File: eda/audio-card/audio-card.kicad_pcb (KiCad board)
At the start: 2 copper layers, 182.4 x 99.1 mm, 13 parts, among them J1 AudioJack2_SwitchT, J2 Bus expansion

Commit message: Interim commit
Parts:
- added U2: 74LS593, Package_DIP:DIP-20_W7.62mm, F.Cu at (100.6, 59.6)
- added U3: 74HCT138, Package_DIP:DIP-16_W10.16mm, F.Cu at (139.7, 125.2)
- added U4: 74HCT574, Package_DIP:DIP-20_W7.62mm, F.Cu at (111.5, 59.6)
- added U5: 74LS593, Package_DIP:DIP-20_W7.62mm, F.Cu at (122.3, 59.6)
- added U6: 74HCT574, Package_DIP:DIP-20_W7.62mm, F.Cu at (133.2, 59.6)
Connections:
- J2 pad 10: /Expansion/D3 -> /Channel/D3
- J2 pad 12: /Expansion/D4 -> /Channel/D4
- J2 pad 14: /Expansion/D5 -> /Channel/D5
- J2 pad 16: /Expansion/D6 -> /Channel/D6
- J2 pad 18: /Expansion/D7 -> /Channel/D7
- J2 pad 36: /Expansion/~{RST} -> /Channel/~{Reset}
- J2 pad 4: /Expansion/D0 -> /Channel/D0
- J2 pad 6: /Expansion/D1 -> /Channel/D1
- J2 pad 8: /Expansion/D2 -> /Channel/D2
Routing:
- net /Expansion/Clock: track 2.79 -> 68.6 mm
- net /Expansion/R~{W}: track 2.79 -> 64.8 mm
- net /Expansion/~{CS}: track 26.7 -> 58.2 mm
- net /Channel/D0: track 0.00 -> 10.7 mm
- net /Channel/D1: track 0.00 -> 10.4 mm
- net /Channel/D3: track 0.00 -> 10.1 mm
- net /Channel/D2: track 0.00 -> 10.1 mm
- net /Channel/D4: track 0.00 -> 9.88 mm
- net /Channel/D5: track 0.00 -> 9.73 mm
- net /Channel/D6: track 0.00 -> 9.48 mm
- net /Channel/D7: track 0.00 -> 9.12 mm
- net /Expansion/A2: track 2.79 -> 11.4 mm
- net /Expansion/A1: track 2.79 -> 11.4 mm
- net /Expansion/A0: track 2.79 -> 11.4 mm
- net /Expansion/D0: track 6.37 -> 0.00 mm
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
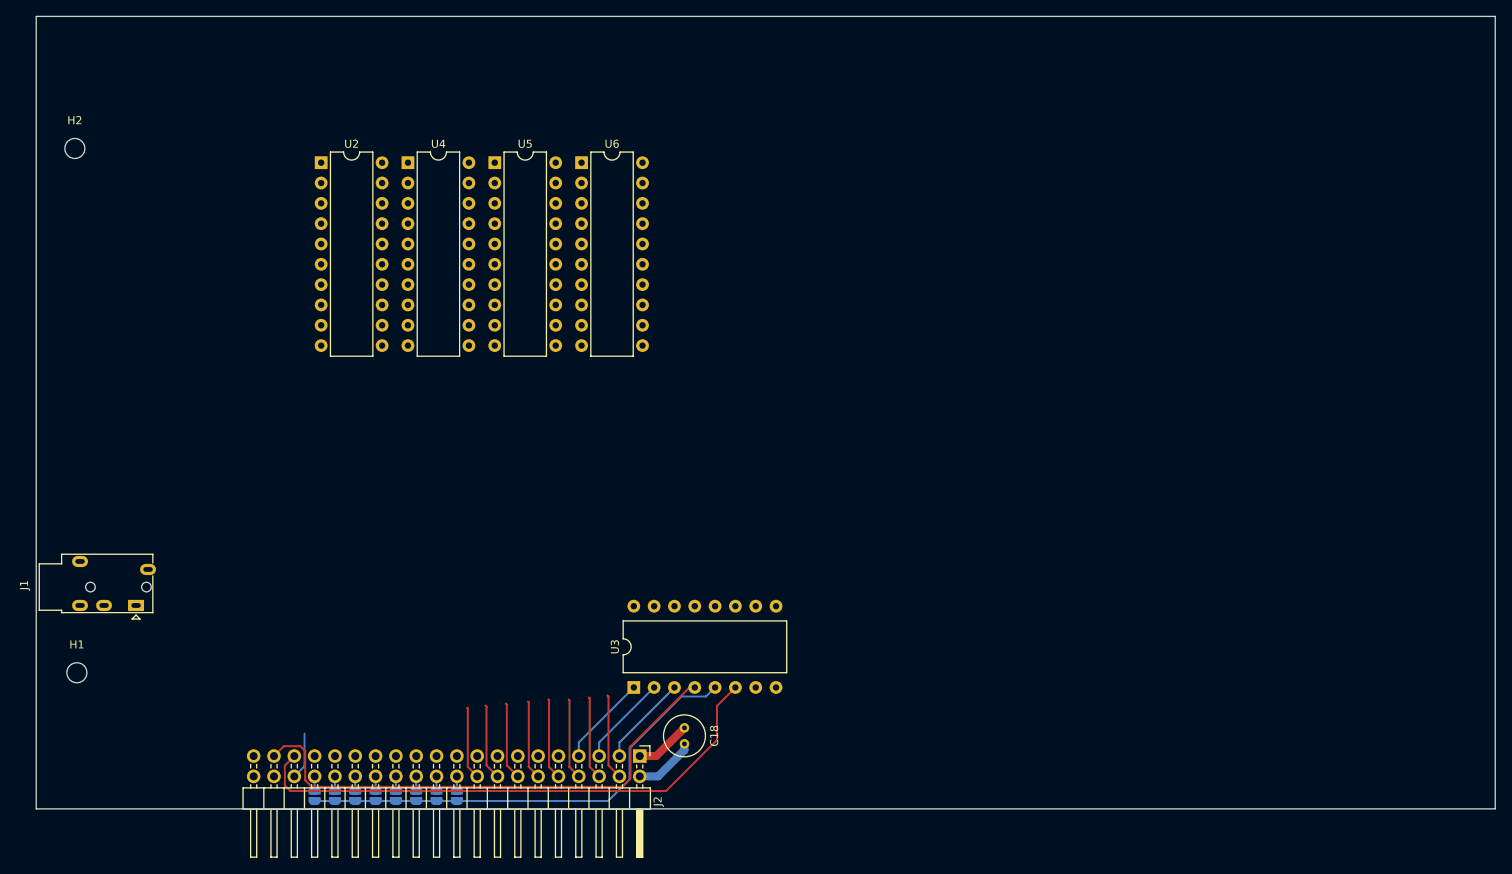
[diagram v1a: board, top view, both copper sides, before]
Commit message: Start converting audio card to analog synth base
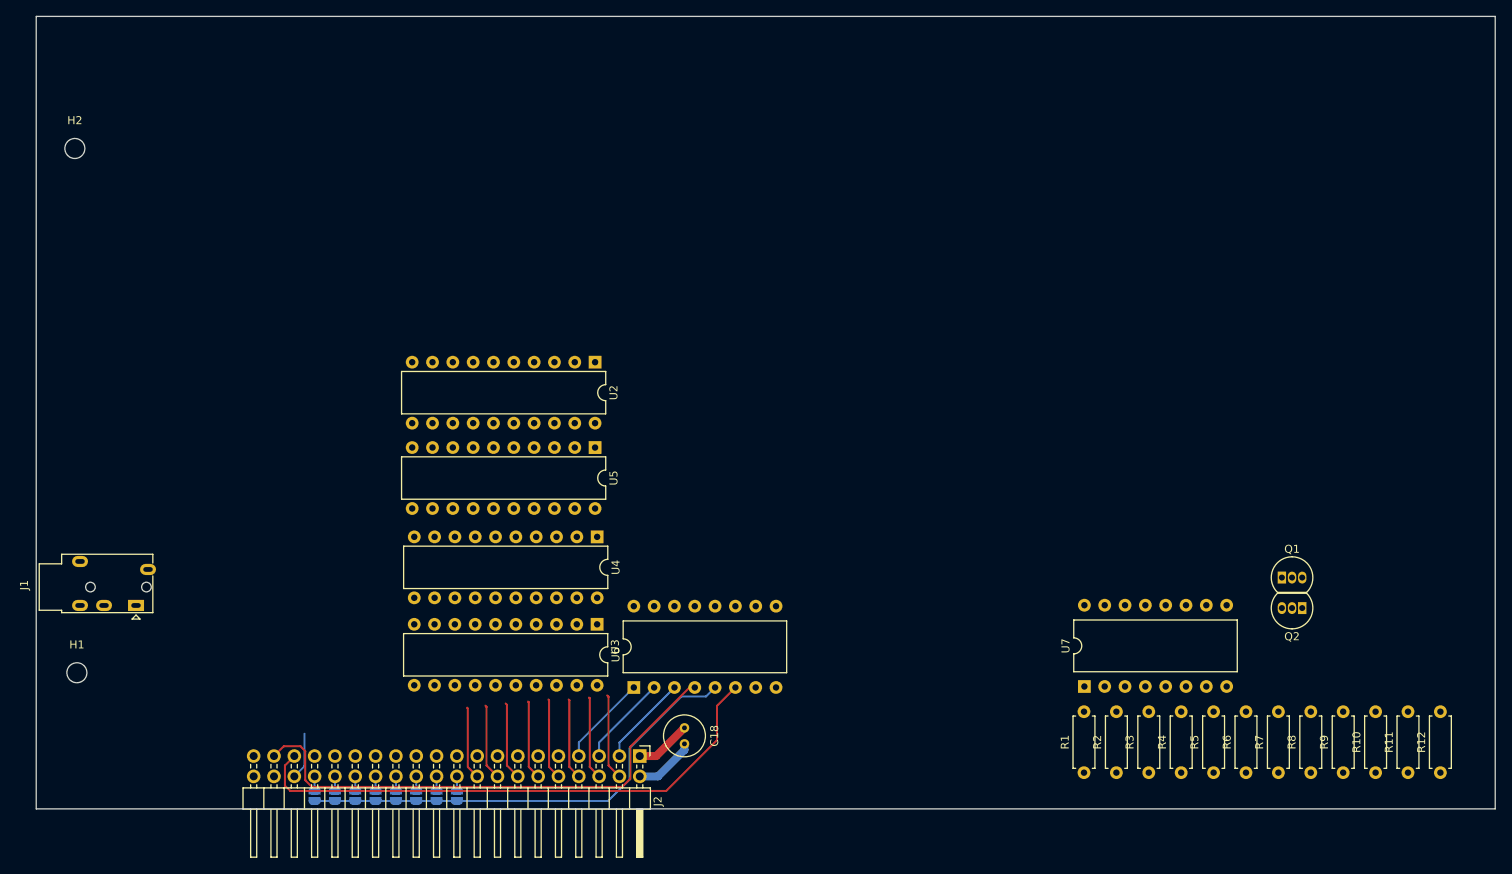
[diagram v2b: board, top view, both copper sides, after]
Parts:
- added Q1: BC558, Package_TO_SOT_THT:TO-92_Inline, F.Cu at (220.7, 111.5)
- added Q2: BC558, Package_TO_SOT_THT:TO-92_Inline, F.Cu at (223.3, 115.3)
- added R1: 100k, Resistor_THT:R_Axial_DIN0207_L6.3mm_D2.5mm_P7.62mm_Horizontal, F.Cu at (196.0, 135.9)
- added R10: 470k, Resistor_THT:R_Axial_DIN0207_L6.3mm_D2.5mm_P7.62mm_Horizontal, F.Cu at (232.4, 135.9)
- added R11: 470k, Resistor_THT:R_Axial_DIN0207_L6.3mm_D2.5mm_P7.62mm_Horizontal, F.Cu at (236.5, 135.9)
- added R12: 1k, Resistor_THT:R_Axial_DIN0207_L6.3mm_D2.5mm_P7.62mm_Horizontal, F.Cu at (240.5, 135.9)
- added R2: 100k, Resistor_THT:R_Axial_DIN0207_L6.3mm_D2.5mm_P7.62mm_Horizontal, F.Cu at (200.0, 135.9)
- added R3: 100k, Resistor_THT:R_Axial_DIN0207_L6.3mm_D2.5mm_P7.62mm_Horizontal, F.Cu at (204.1, 135.9)
- added R4: 100R, Resistor_THT:R_Axial_DIN0207_L6.3mm_D2.5mm_P7.62mm_Horizontal, F.Cu at (208.1, 135.9)
- added R5: 200k, Resistor_THT:R_Axial_DIN0207_L6.3mm_D2.5mm_P7.62mm_Horizontal, F.Cu at (212.2, 135.9)
- added R6: 33k, Resistor_THT:R_Axial_DIN0207_L6.3mm_D2.5mm_P7.62mm_Horizontal, F.Cu at (216.2, 135.9)
- added R7: 10k, Resistor_THT:R_Axial_DIN0207_L6.3mm_D2.5mm_P7.62mm_Horizontal, F.Cu at (220.3, 135.9)
- added R8: 10k, Resistor_THT:R_Axial_DIN0207_L6.3mm_D2.5mm_P7.62mm_Horizontal, F.Cu at (224.3, 135.9)
- added R9: 10k, Resistor_THT:R_Axial_DIN0207_L6.3mm_D2.5mm_P7.62mm_Horizontal, F.Cu at (228.4, 135.9)
- added U7: TL074, Package_DIP:DIP-16_W10.16mm, F.Cu at (196.0, 125.1)
- U2, U5: value 74LS593 -> 74HCT574
- moved U6 57.7 mm to (135.1, 117.3), turned to -90 degrees
- moved U4 52.4 mm to (135.1, 106.4), turned to -90 degrees
- moved U2 42.4 mm to (134.9, 84.6), turned to -90 degrees
- moved U5 37.7 mm to (134.9, 95.2), turned to -90 degrees
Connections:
- net Net-(U1A-C) renamed /Channel/~{EnvelopeLatch}
- U2 pad 1: Net-(U2-A) -> GND
- U2 pad 11: Net-(U2-~{RCO}) -> /Channel/~{NoteLatch}
- U2 pad 12: /Channel/~{Reset} -> unconnected-(U2-Q7-Pad12)
- U2 pad 13: /Channel/MainClock -> unconnected-(U2-Q6-Pad13)
- U2 pad 14: GND -> unconnected-(U2-Q5-Pad14)
- U2 pad 16: VCC -> unconnected-(U2-Q3-Pad16)
- U2 pad 17: /Channel/~{NoteLatch} -> unconnected-(U2-Q2-Pad17)
- U2 pad 2: Net-(U2-B) -> /Channel/D0
- U2 pad 3: Net-(U2-C) -> /Channel/D1
- U2 pad 4: Net-(U2-D) -> /Channel/D2
- U2 pad 5: Net-(U2-E) -> /Channel/D3
- U2 pad 6: (no net) -> /Channel/D4
- U2 pad 7: Net-(U2-F) -> /Channel/D5
- U2 pad 8: Net-(U2-H) -> /Channel/D6
- U2 pad 9: /Channel/~{Reset} -> /Channel/D7
- U4 pad 1: /Channel/Tone -> GND
- U4 pad 2: unconnected-(U4-D0-Pad2) -> /Channel/D0
- U4 pad 3: unconnected-(U4-D1-Pad3) -> /Channel/D1
- U4 pad 4: unconnected-(U4-D2-Pad4) -> /Channel/D2
- U4 pad 5: unconnected-(U4-D3-Pad5) -> /Channel/D3
- U4 pad 6: unconnected-(U4-D4-Pad6) -> /Channel/D4
- U4 pad 7: unconnected-(U4-D5-Pad7) -> /Channel/D5
- U4 pad 8: unconnected-(U4-D6-Pad8) -> /Channel/D6
- U4 pad 9: unconnected-(U4-D7-Pad9) -> /Channel/D7
- U5 pad 1: /Channel/D0 -> GND
- U5 pad 12: /Channel/~{Reset} -> unconnected-(U5-Q7-Pad12)
- U5 pad 13: VCC -> unconnected-(U5-Q6-Pad13)
- U5 pad 14: Net-(U2-~{RCO}) -> unconnected-(U5-Q5-Pad14)
- U5 pad 15: VCC -> unconnected-(U5-Q4-Pad15)
- U5 pad 16: VCC -> unconnected-(U5-Q3-Pad16)
- U5 pad 17: /Channel/~{NoteLatch} -> unconnected-(U5-Q2-Pad17)
- U5 pad 2: /Channel/D1 -> /Channel/D0
- U5 pad 3: /Channel/D2 -> /Channel/D1
- U5 pad 4: /Channel/D3 -> /Channel/D2
- U5 pad 5: /Channel/D4 -> /Channel/D3
- U5 pad 6: (no net) -> /Channel/D4
- U5 pad 8: /Channel/D7 -> /Channel/D6
- U5 pad 9: /Channel/~{Reset} -> /Channel/D7
- U6 pad 12: Net-(U2-H) -> unconnected-(U6-Q7-Pad12)
- U6 pad 13: Net-(U6-Q6) -> unconnected-(U6-Q6-Pad13)
- U6 pad 14: Net-(U2-F) -> unconnected-(U6-Q5-Pad14)
- U6 pad 15: Net-(U2-E) -> unconnected-(U6-Q4-Pad15)
- U6 pad 16: Net-(U2-D) -> unconnected-(U6-Q3-Pad16)
- U6 pad 17: Net-(U2-C) -> unconnected-(U6-Q2-Pad17)
- U6 pad 18: Net-(U2-B) -> unconnected-(U6-Q1-Pad18)
- U6 pad 19: Net-(U2-A) -> unconnected-(U6-Q0-Pad19)
